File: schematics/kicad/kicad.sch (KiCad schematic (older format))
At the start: 5 parts

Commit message: bugfixes, updated schematic
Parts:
- added L?: HT7333-A, symbol ht7333-a:HT7333-A
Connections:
- net at D?.1 (K), U?.15 (GND), U?.2 (GND): now also L?.1 (GND)
- net at U?.8 (VCC): now also L?.3 (VOUT)
- new net +3V3: L?.2 (VIN)
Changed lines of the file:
@@
 Wire Wire Line
 	6350 5550 6150 5550
+$Comp
+L ht7333-a:HT7333-A L?
+U 1 1 617A55A2
+P 5400 2600
+F 0 "L?" H 5450 2997 60  0000 C CNN
+F 1 "HT7333-A" H 5450 2891 60  0000 C CNN
+F 2 "" H 5400 2600 60  0000 C CNN
+F 3 "" H 5400 2600 60  0000 C CNN
+	1    5400 2600
+	1    0    0    -1
+$EndComp
+Wire Wire Line
+	5900 2450 5900 3450
+Wire Wire Line
+	5900 3450 5550 3450
+Wire Wire Line
+	5550 2900 4200 2900
+Wire Wire Line
+	4200 2900 4200 5150
+Wire Wire Line
+	4200 5150 5550 5150
+$Comp
+L power:+3.3V #PWR?
+U 1 1 617A7405
+P 4800 2450
+F 0 "#PWR?" H 4800 2300 50  0001 C CNN
+F 1 "+3.3V" H 4815 2623 50  0000 C CNN
+F 2 "" H 4800 2450 50  0001 C CNN
+F 3 "" H 4800 2450 50  0001 C CNN
+	1    4800 2450
+	1    0    0    -1
+$EndComp
+Wire Wire Line
+	4800 2450 4800 2600
+Wire Wire Line
+	4800 2600 5000 2600
 $EndSCHEMATC

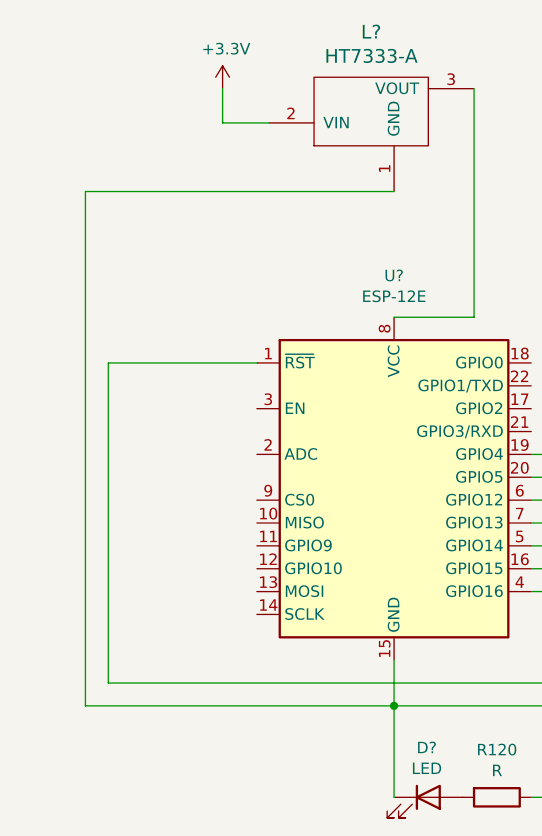
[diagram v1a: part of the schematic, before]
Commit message: Add battery monitor
* battery level is published via mqtt
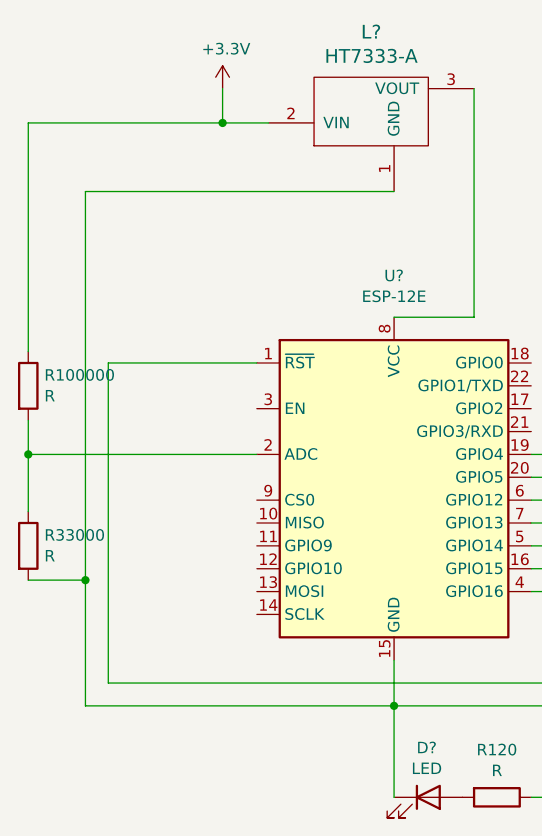
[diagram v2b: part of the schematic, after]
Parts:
- added R100000, R33000: R, symbol Device:R
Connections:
- net +3V3: now also R100000.1
- net at D?.1 (K), L?.1 (GND), U?.15 (GND)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: now also R33000.2
- net at U?.2 (ADC): now also R100000.2, R33000.1
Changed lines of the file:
@@
 encoding utf-8
 Sheet 1 1
-Title ""
-Date ""
-Rev ""
-Comp ""
+Title "Open-Heat ESP12-E schematic"
+Date "2021-11-06"
+Rev "0.1"
+Comp "Alexander Mohr"
 Comment1 ""
 Comment2 ""
@@
 	5550 2900 4200 2900
 Wire Wire Line
-	4200 2900 4200 5150
+	4200 2900 4200 4600
 Wire Wire Line
 	4200 5150 5550 5150
@@
 $EndComp
 Wire Wire Line
+	3950 3900 3950 4050
+$Comp
+L Device:R R33000
+U 1 1 6186F150
+P 3950 4450
+F 0 "R33000" H 4020 4496 50  0000 L CNN
+F 1 "R" H 4020 4405 50  0000 L CNN
+F 2 "" V 3880 4450 50  0001 C CNN
+F 3 "~" H 3950 4450 50  0001 C CNN
+	1    3950 4450
+	1    0    0    -1
+$EndComp
+$Comp
+L Device:R R100000
+U 1 1 6186E03C
+P 3950 3750
+F 0 "R100000" H 4020 3796 50  0000 L CNN
+F 1 "R" H 4020 3705 50  0000 L CNN
+F 2 "" V 3880 3750 50  0001 C CNN
+F 3 "~" H 3950 3750 50  0001 C CNN
+	1    3950 3750
+	1    0    0    -1
+$EndComp
+Wire Wire Line
+	4950 4050 3950 4050
+Wire Wire Line
+	3950 4300 3950 4050
+Connection ~ 3950 4050
+Wire Wire Line
+	3950 2600 3950 3600
+Wire Wire Line
+	3950 2600 4800 2600
+Wire Wire Line
 	4800 2450 4800 2600
+Connection ~ 4800 2600
 Wire Wire Line
 	4800 2600 5000 2600
+Wire Wire Line
+	3950 4600 4200 4600
+Connection ~ 4200 4600
+Wire Wire Line
+	4200 4600 4200 5150
 $EndSCHEMATC

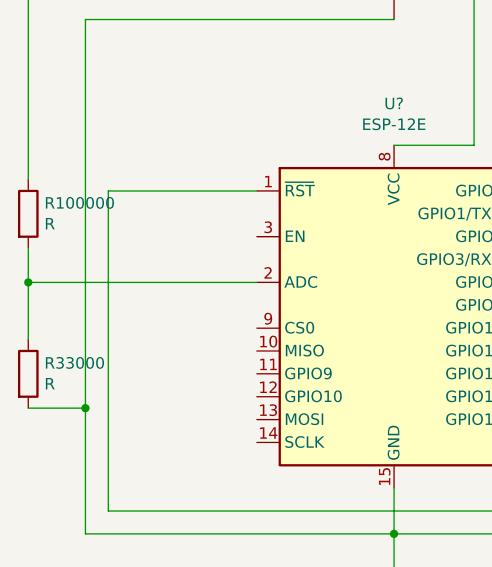
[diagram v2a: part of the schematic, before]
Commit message: update readme, schematics and voltage divider
* remove curl commands from readme. Configuration is only possible via
  ui now
* update schematics and voltage divider to show and use 10m and 3.3M
  resistors. This should reduce the battery drain due to the voltage
  monitoring.
  100k and 33k still can be used with the same code because the relation
  stays the same
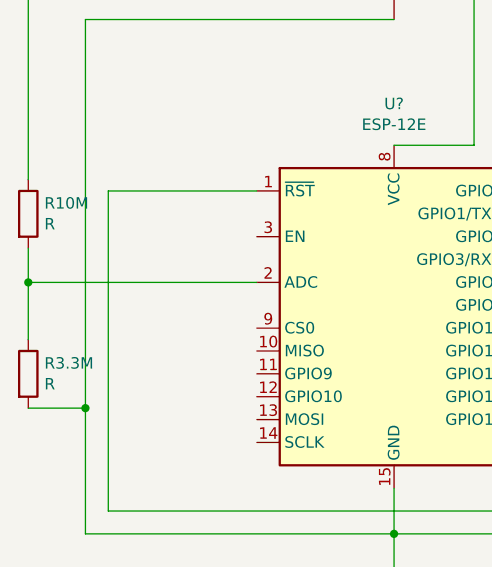
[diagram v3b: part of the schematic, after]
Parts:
- renumbered R100000 to R10M, R33000 to R3.3M
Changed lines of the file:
@@
 	3950 3900 3950 4050
 $Comp
-L Device:R R33000
+L Device:R R3.3M
 U 1 1 6186F150
 P 3950 4450
-F 0 "R33000" H 4020 4496 50  0000 L CNN
+F 0 "R3.3M" H 4020 4496 50  0000 L CNN
 F 1 "R" H 4020 4405 50  0000 L CNN
 F 2 "" V 3880 4450 50  0001 C CNN
@@
 $EndComp
 $Comp
-L Device:R R100000
+L Device:R R10M
 U 1 1 6186E03C
 P 3950 3750
-F 0 "R100000" H 4020 3796 50  0000 L CNN
+F 0 "R10M" H 4020 3796 50  0000 L CNN
 F 1 "R" H 4020 3705 50  0000 L CNN
 F 2 "" V 3880 3750 50  0001 C CNN
